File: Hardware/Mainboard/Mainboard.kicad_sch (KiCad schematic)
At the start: 81 parts, among them J1 Conn_01x04_Pin, J2 USB_C_Receptacle_USB2.0_16P, Q1 NMOS, Q2 NMOS, U1 ESP32-S2-SOLO-2

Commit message: Completed sample rev A. Requires Review.
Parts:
- removed Q1, Q2: NMOS, symbol Simulation_SPICE:NMOS
- removed R4: 1M, symbol Device:R_Small
- added C2, C6: 10u, Capacitor_SMD:C_0603_1608Metric, symbol Device:C_Small
- added C3, C4: 22u, Capacitor_SMD:C_0805_2012Metric, symbol Device:C_Small
- added C5: 6p3, Capacitor_SMD:C_0402_1005Metric, symbol Device:C_Small
- added L1: 2u2, Inductor_SMD:L_Cenker_CKCS4018, symbol Device:L
- added Q1, Q2: Q_NMOS_GDS, Package_TO_SOT_SMD:TO-252-2, symbol Device:Q_NMOS_GDS
- added R35: 470k, Resistor_SMD:R_0402_1005Metric, symbol Device:R_Small
- added R36: 100k, Resistor_SMD:R_0402_1005Metric, symbol Device:R_Small
- added SW1, SW2: SW_Push, Button_Switch_SMD:SW_SPST_SKQG_WithStem, symbol Switch:SW_Push
- added TP2, TP3, TP4, TP5: TestPoint, TestPoint:TestPoint_Pad_D1.5mm, symbol Connector:TestPoint
- added U2: TLV62569DBV, Package_TO_SOT_SMD:SOT-23-5, symbol Regulator_Switching:TLV62569DBV
- C1: value 1u -> 100n; footprint Capacitor_SMD:C_0603_1608Metric -> Capacitor_SMD:C_0402_1005Metric
- D1, D10, D11, D12, D13, D14, D15, D16, D17, D18, D19, D2, D20, D21, D22, D23, D24, D25, D26, D27, D28, D29, D3, D30, D4, D5, D6, D7, D8, D9: footprint (none) -> LED_SMD:LED_PLCC_2835
- J1: footprint (none) -> Connector_PinHeader_2.54mm:PinHeader_1x04_P2.54mm_Vertical
- J2: footprint (none) -> USB_Connector_Custom:XKB_U263-14XN-5XQC14
- R10, R11, R12, R13, R14, R15, R16, R17, R18, R19, R20, R21, R22, R23, R24, R25, R26, R27, R28, R29, R30, R31, R32, R33, R34, R5, R6, R7, R8, R9: footprint (none) -> Resistor_SMD:R_0603_1608Metric
- TP1: footprint (none) -> TestPoint:TestPoint_Pad_D1.0mm
- U1: footprint (none) -> RF_Module:ESP32-S3-WROOM-1
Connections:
- net +3V3: now also D31.4 (VDD), D32.4 (VDD), D33.4 (VDD), D34.4 (VDD), D35.4 (VDD), D36.4 (VDD), D37.4 (VDD), D38.4 (VDD), D39.4 (VDD), D40.4 (VDD), R1.2, R10.1, R11.1, R12.1, R13.1, R14.1, R15.1, R16.1, R17.1, R18.1, R19.1, R20.1, R21.1, R22.1, R23.1, R24.1, R25.1, R26.1, R27.1, R28.1, R29.1, R30.1, R31.1, R32.1, R33.1, R34.1, R5.1, R6.1, R7.1, R8.1, R9.1, C3.1, C4.1, C5.1, C6.1, L1.2, R35.1; no longer C1.2, R1.1
- net +5V: now also C2.1, U2.1 (EN), U2.4 (VIN); no longer D1.2 (A), D10.2 (A), D11.2 (A), D12.2 (A), D13.2 (A), D14.2 (A), D15.2 (A), D16.2 (A), D17.2 (A), D18.2 (A), D19.2 (A), D2.2 (A), D20.2 (A), D21.2 (A), D22.2 (A), D23.2 (A), D24.2 (A), D25.2 (A), D26.2 (A), D27.2 (A), D28.2 (A), D29.2 (A), D3.2 (A), D30.2 (A), D31.4 (VDD), D32.4 (VDD), D33.4 (VDD), D34.4 (VDD), D35.4 (VDD), D36.4 (VDD), D37.4 (VDD), D38.4 (VDD), D39.4 (VDD), D4.2 (A), D40.4 (VDD), D5.2 (A), D6.2 (A), D7.2 (A), D8.2 (A), D9.2 (A)
- net CTRL_1800k: now also U1.31 (IO38), Q1.1 (G); no longer U1.6 (IO6)
- net CTRL_3000k: now also U1.29 (IO36), Q2.1 (G); no longer U1.8 (IO15)
- net GND: now also J2.S1 (SHIELD), C2.2, C3.2, C4.2, C6.2, Q1.3 (S), Q2.3 (S), R36.2, SW1.2, SW2.2, U2.2 (GND)
- net at D21.1 (K): now also D22.1 (K), D23.1 (K), D24.1 (K), D25.1 (K), D26.1 (K), D27.1 (K), D28.1 (K), D29.1 (K), D30.1 (K), Q1.2 (D); no longer R25.1
- net at D11.1 (K): now also D1.1 (K), D10.1 (K), D12.1 (K), D13.1 (K), D14.1 (K), D15.1 (K), D16.1 (K), D17.1 (K), D18.1 (K), D19.1 (K), D2.1 (K), D20.1 (K), D3.1 (K), D4.1 (K), D5.1 (K), D6.1 (K), D7.1 (K), D8.1 (K), D9.1 (K), Q2.2 (D); no longer R15.1
- net RST: now reaches U1.3 (EN)
- net RST: now also C1.2, R1.1, SW2.1; no longer R1.2
- net at U1.19 (IO11): now also TP5.1
- net at U1.21 (IO13): now also TP4.1
- net at U1.23 (IO21): now also TP3.1
- net at U1.25 (IO34): now also TP2.1
- net at U1.27 (IO0): now also SW1.1
- new net: D25.2 (A), R29.2
- new net: D29.2 (A), R33.2
- new net: D11.2 (A), R15.2
- new net: D28.2 (A), R32.2
- new net: D12.2 (A), R16.2
- new net: D15.2 (A), R19.2
- new net: D24.2 (A), R28.2
- new net: D18.2 (A), R22.2
- new net: D13.2 (A), R17.2
- new net: D1.2 (A), R5.2
- new net: D26.2 (A), R30.2
- new net: D19.2 (A), R23.2
- new net: C5.2, R35.2, R36.1, U2.5 (FB)
- new net: D30.2 (A), R34.2
- new net: D14.2 (A), R18.2
- new net: D10.2 (A), R14.2
- new net: D3.2 (A), R7.2
- new net: D16.2 (A), R20.2
- new net: D27.2 (A), R31.2
- new net: L1.1, U2.3 (SW)
- new net: D8.2 (A), R12.2
- new net: D20.2 (A), R24.2
- new net: D21.2 (A), R25.2
- new net: D9.2 (A), R13.2
- new net: D7.2 (A), R11.2
- new net: D6.2 (A), R10.2
- new net: D22.2 (A), R26.2
- new net: D5.2 (A), R9.2
- new net: D4.2 (A), R8.2
- new net: D2.2 (A), R6.2
- new net: D17.2 (A), R21.2
- new net: D23.2 (A), R27.2
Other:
- note added: "BUCK Converter"
- note added: "Bank of 10x RGB LEDs (Neopixel). These are included for fun. No plans. Firelight? Flicker?"
- note added: "Bank of 10x ~1800K (red/amber) LEDs. Should be limited to 50mA draw per LED. These are to provide the nighttime illumination."
- note added: "Bank of 20x 3000K (Warm[er] White) LEDs. Should be limited to 50mA draw per LED. These are to provide the primary illumination."
- note added: "Drops +5V from USB to about +3.3v for the LEDs. More efficient than dumping power into resistors. Care about low heating. LEDs get hot."
- note added: "Potentiometer will hit a test point and use the debug serial port for power."
- note added: "Strapping"
- moved on the sheet: D1, D10, D11, D12, D13, D14, D15, D16, D17, D18, D19, D2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

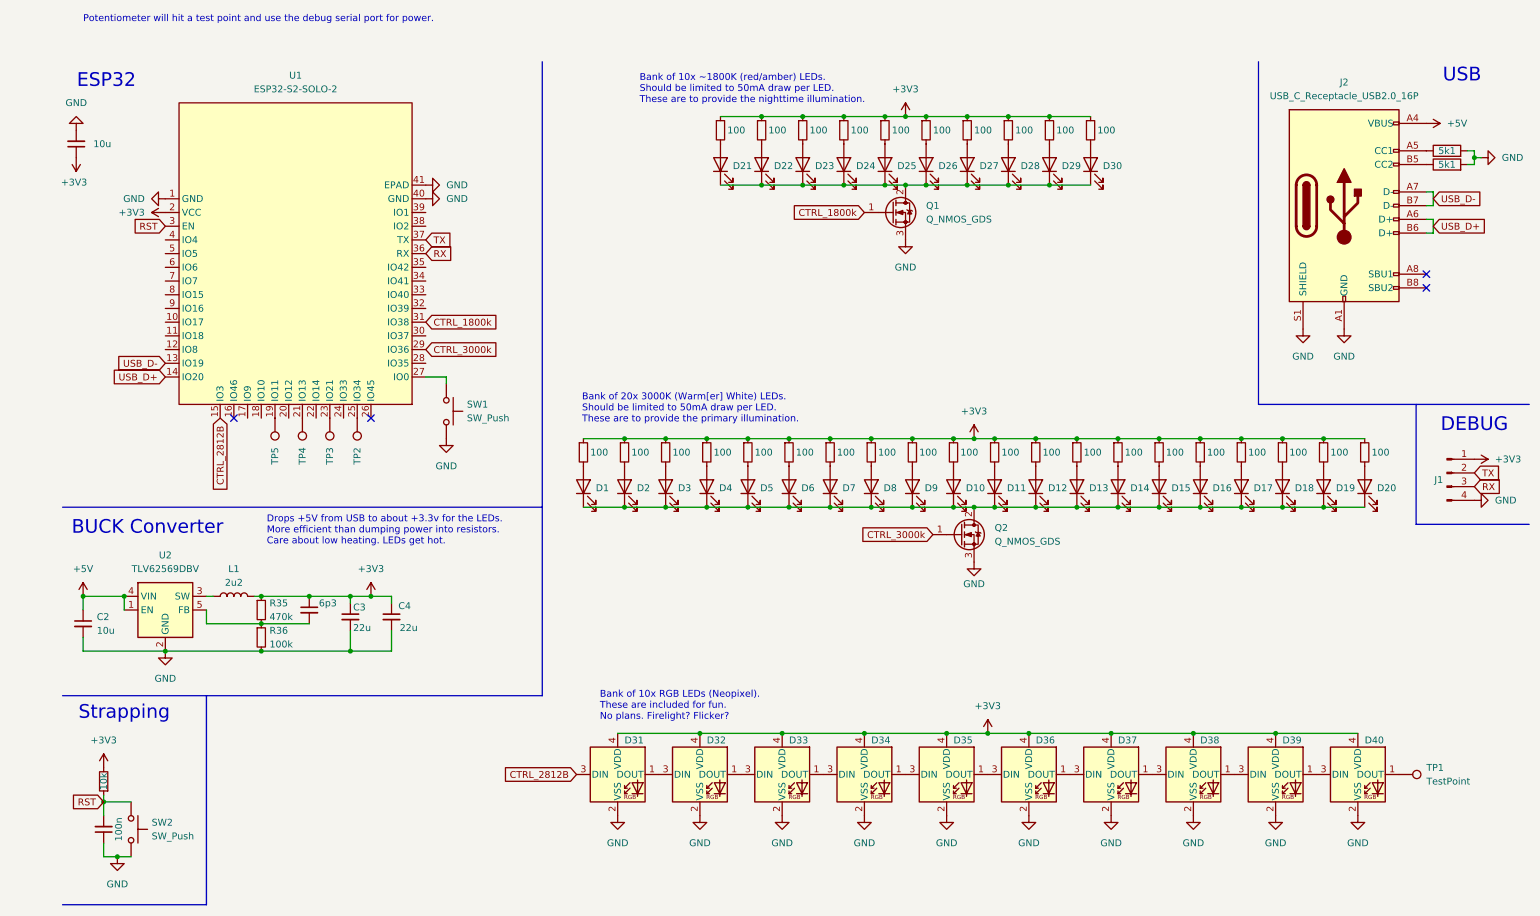
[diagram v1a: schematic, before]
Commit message: Finalize layout, silkscreen, outline. Pending review
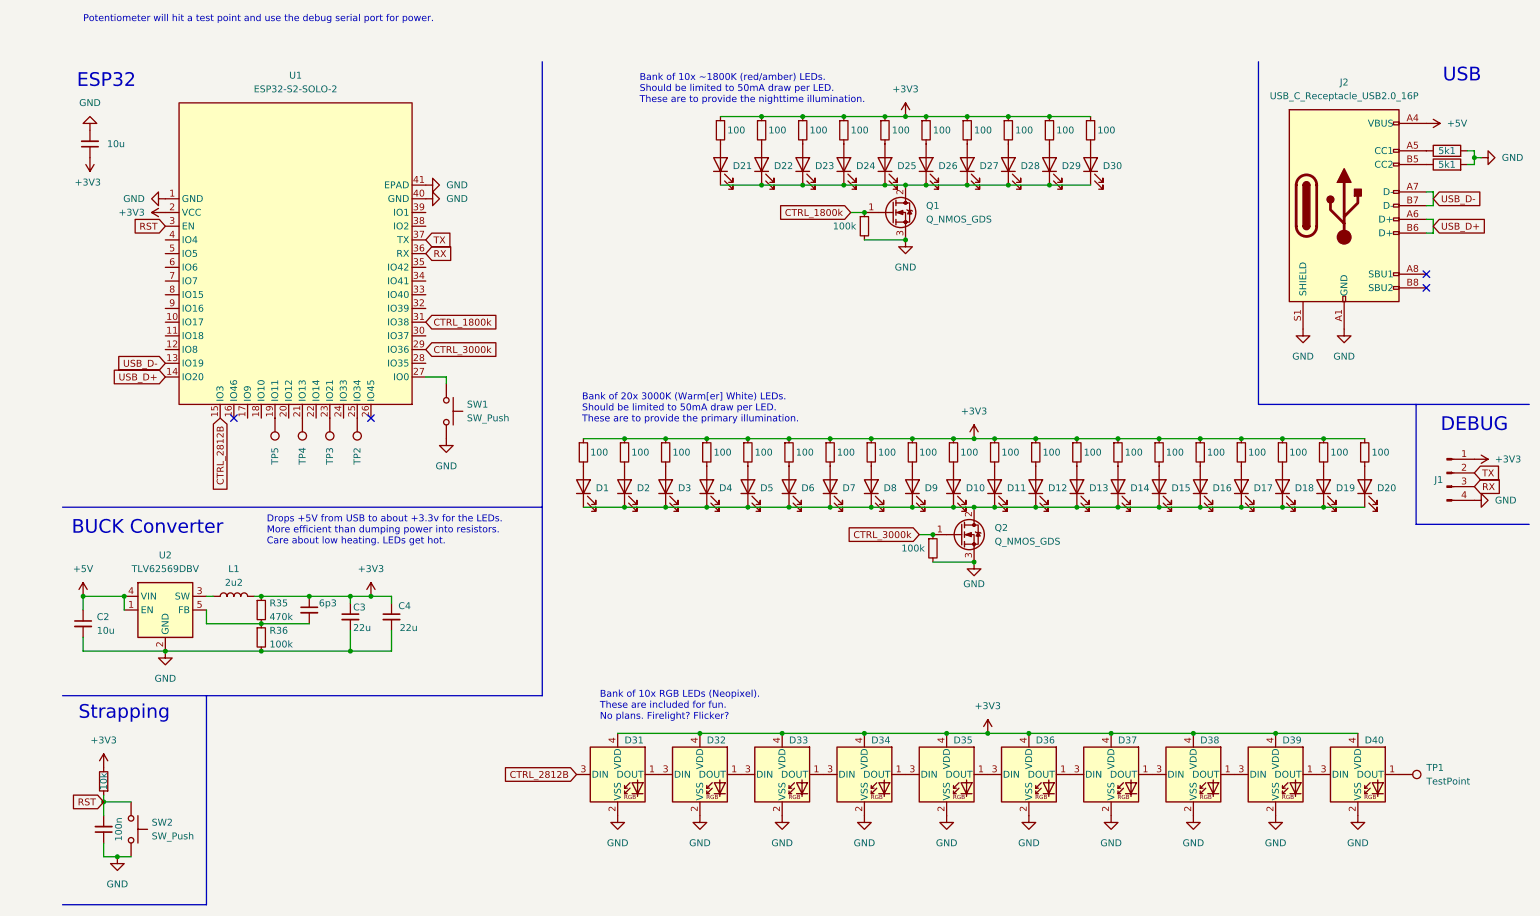
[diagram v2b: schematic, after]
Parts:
- added R37, R4: 100k, Resistor_SMD:R_0603_1608Metric, symbol Device:R_Small
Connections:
- net CTRL_1800k: now also R37.1
- net CTRL_3000k: now also R4.1
- net GND: now also R37.2, R4.2
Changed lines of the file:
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@@
 	)
 	(junction
+		(at 173.99 100.33)
+		(diameter 0)
+		(color 0 0 0 0)
+	)
+	(junction
 		(at 200.66 95.25)
 		(diameter 0)
@@
 	)
 	(junction
+		(at 168.91 45.72)
+		(diameter 0)
+		(color 0 0 0 0)
+	)
+	(junction
 		(at 139.7 82.55)
 		(diameter 0)
@@
 	)
 	(junction
+		(at 161.29 40.64)
+		(diameter 0)
+		(color 0 0 0 0)
+	)
+	(junction
+		(at 181.61 105.41)
+		(diameter 0)
+		(color 0 0 0 0)
+	)
+	(junction
 		(at 238.76 95.25)
 		(diameter 0)
@@
 	(wire
 		(pts
+			(xy 161.29 45.72) (xy 168.91 45.72)
+		)
+		(stroke
+			(width 0)
+			(type default)
+		)
+	)
+	(wire
+		(pts
 			(xy 66.04 118.11) (xy 66.04 121.92)
 		)
@@
 	(wire
 		(pts
+			(xy 173.99 105.41) (xy 181.61 105.41)
+		)
+		(stroke
+			(width 0)
+			(type default)
+		)
+	)
+	(wire
+		(pts
 			(xy 265.43 44.45) (xy 266.7 44.45)
 		)
@@
 	(wire
 		(pts
+			(xy 171.45 100.33) (xy 173.99 100.33)
+		)
+		(stroke
+			(width 0)
+			(type default)
+		)
+	)
+	(wire
+		(pts
 			(xy 116.84 95.25) (xy 124.46 95.25)
 		)
@@
 	(wire
 		(pts
+			(xy 158.75 40.64) (xy 161.29 40.64)
+		)
+		(stroke
+			(width 0)
+			(type default)
+		)
+	)
+	(wire
+		(pts
 			(xy 266.7 41.91) (xy 266.7 44.45)
 		)
@@
 	(global_label "CTRL_1800k"
 		(shape input)
-		(at 161.29 40.64 180)
+		(at 158.75 40.64 180)
 		(fields_autoplaced yes)
 		(effects
@@
 		)
 		(property "Intersheetrefs" "${INTERSHEET_REFS}"
-			(at 146.9354 40.64 0)
+			(at 144.3954 40.64 0)
 			(effects
 				(font
@@
 	(global_label "CTRL_3000k"
 		(shape input)
-		(at 173.99 100.33 180)
+		(at 171.45 100.33 180)
 		(fields_autoplaced yes)
 		(effects
@@
 		)
 		(property "Intersheetrefs" "${INTERSHEET_REFS}"
-			(at 159.6354 100.33 0)
+			(at 157.0954 100.33 0)
 			(effects
 				(font
@@
 	(symbol
 		(lib_id "Device:R_Small")
+		(at 161.29 43.18 0)
+		(unit 1)
+		(exclude_from_sim no)
+		(in_bom yes)
+		(on_board yes)
+		(dnp no)
+		(property "Reference" "R37"
+			(at 163.83 41.9099 0)
+			(effects
+				(font
+					(size 1.27 1.27)
+				)
+				(justify left)
+				(hide yes)
+			)
+		)
+		(property "Value" "100k"
+			(at 155.448 43.18 0)
+			(effects
+				(font
+					(size 1.27 1.27)
+				)
+				(justify left)
+			)
+		)
+		(property "Footprint" "Resistor_SMD:R_0603_1608Metric"
+			(at 161.29 43.18 0)
+			(effects
+				(font
+					(size 1.27 1.27)
+				)
+				(hide yes)
+			)
+		)
+		(property "Datasheet" "~"
+			(at 161.29 43.18 0)
+			(effects
+				(font
+					(size 1.27 1.27)
+				)
+				(hide yes)
+			)
+		)
+		(property "Description" "Resistor, small symbol"
+			(at 161.29 43.18 0)
+			(effects
+				(font
+					(size 1.27 1.27)
+				)
+				(hide yes)
+			)
+		)
+		(pin "1"
+		)
+		(pin "2"
+		)
+		(instances
+			(project "Mainboard"
+				(path "/614c0474-1679-4dec-b558-2d0f66e85378"
+					(reference "R37")
+					(unit 1)
+				)
+			)
+		)
+	)
+	(symbol
+		(lib_id "Device:R_Small")
 		(at 20.32 146.05 180)
 		(unit 1)
@@
 	)
 	(symbol
+		(lib_id "Device:R_Small")
+		(at 173.99 102.87 0)
+		(unit 1)
+		(exclude_from_sim no)
+		(in_bom yes)
+		(on_board yes)
+		(dnp no)
+		(property "Reference" "R4"
+			(at 176.53 101.5999 0)
+			(effects
+				(font
+					(size 1.27 1.27)
+				)
+				(justify left)
+				(hide yes)
+			)
+		)
+		(property "Value" "100k"
+			(at 168.148 102.87 0)
+			(effects
+				(font
+					(size 1.27 1.27)
+				)
+				(justify left)
+			)
+		)
+		(property "Footprint" "Resistor_SMD:R_0603_1608Metric"
+			(at 173.99 102.87 0)
+			(effects
+				(font
+					(size 1.27 1.27)
+				)
+				(hide yes)
+			)
+		)
+		(property "Datasheet" "~"
+			(at 173.99 102.87 0)
+			(effects
+				(font
+					(size 1.27 1.27)
+				)
+				(hide yes)
+			)
+		)
+		(property "Description" "Resistor, small symbol"
+			(at 173.99 102.87 0)
+			(effects
+				(font
+					(size 1.27 1.27)
+				)
+				(hide yes)
+			)
+		)
+		(pin "1"
+		)
+		(pin "2"
+		)
+		(instances
+			(project ""
+				(path "/614c0474-1679-4dec-b558-2d0f66e85378"
+					(reference "R4")
+					(unit 1)
+				)
+			)
+		)
+	)
+	(symbol
 		(lib_id "LED:WS2812B-2020")
 		(at 207.01 144.78 0)
@@
 	(symbol
 		(lib_id "power:+3V3")
-		(at 15.24 30.48 180)
+		(at 17.78 30.48 180)
 		(unit 1)
 		(exclude_from_sim no)
@@
 		(dnp no)
 		(property "Reference" "#PWR020"
-			(at 15.24 26.67 0)
+			(at 17.78 26.67 0)
 			(effects
 				(font
@@
 		)
 		(property "Value" "+3V3"
-			(at 17.272 35.052 0)
+			(at 19.812 35.052 0)
 			(effects
 				(font
@@
 		)
 		(property "Footprint" ""
-			(at 15.24 30.48 0)
+			(at 17.78 30.48 0)
 			(effects
 				(font
@@
 		)
 		(property "Datasheet" ""
-			(at 15.24 30.48 0)
+			(at 17.78 30.48 0)
 			(effects
 				(font
@@
 		)
 		(property "Description" "Power symbol creates a global label with name \"+3V3\""
-			(at 15.24 30.48 0)
+			(at 17.78 30.48 0)
 			(effects
 				(font
@@
 	(symbol
 		(lib_id "Device:C_Small")
-		(at 15.24 27.94 180)
+		(at 17.78 27.94 180)
 		(unit 1)
 		(exclude_from_sim no)
@@
 		(dnp no)
 		(property "Reference" "C6"
-			(at 8.89 27.9337 90)
+			(at 11.43 27.9337 90)
 			(effects
 				(font
@@
 		)
 		(property "Value" "10u"
-			(at 20.066 27.94 0)
+			(at 22.606 27.94 0)
 			(effects
 				(font
@@
 		)
 		(property "Footprint" "Capacitor_SMD:C_0603_1608Metric"
-			(at 15.24 27.94 0)
+			(at 17.78 27.94 0)
 			(effects
 				(font
@@
 		)
 		(property "Datasheet" "~"
-			(at 15.24 27.94 0)
+			(at 17.78 27.94 0)
 			(effects
 				(font
@@
 		)
 		(property "Description" "Unpolarized capacitor, small symbol"
-			(at 15.24 27.94 0)
+			(at 17.78 27.94 0)
 			(effects
 				(font
@@
 	(symbol
 		(lib_id "power:GND")
-		(at 15.24 25.4 180)
+		(at 17.78 25.4 180)
 		(unit 1)
 		(exclude_from_sim no)
@@
 		(fields_autoplaced yes)
 		(property "Reference" "#PWR05"
-			(at 15.24 19.05 0)
+			(at 17.78 19.05 0)
 			(effects
 				(font
@@
 		)
 		(property "Value" "GND"
-			(at 15.24 20.32 0)
+			(at 17.78 20.32 0)
 			(effects
 				(font
@@
 		)
 		(property "Footprint" ""
-			(at 15.24 25.4 0)
+			(at 17.78 25.4 0)
 			(effects
 				(font
@@
 		)
 		(property "Datasheet" ""
-			(at 15.24 25.4 0)
+			(at 17.78 25.4 0)
 			(effects
 				(font
@@
 		)
 		(property "Description" "Power symbol creates a global label with name \"GND\" , ground"
-			(at 15.24 25.4 0)
+			(at 17.78 25.4 0)
 			(effects
 				(font
